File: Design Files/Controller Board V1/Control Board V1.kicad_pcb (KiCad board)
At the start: 4 copper layers, 75 x 125 mm, 72 parts, among them J1 XT30PW-F, J10 SM04B-GHS-TB_LF__SN_-, J11 SM04B-GHS-TB_LF__SN_-, J2 XT30UPB-M, J3 XT30UPB-M, J4 XT30UPB-M, J5 XT30UPB-M, J6 XT30UPB-M, J7 XT30UPB-M, J8 SM04B-GHS-TB_LF__SN_-, J9 SM04B-GHS-TB_LF__SN_-, Q1 LMG5200, U1 LMR51420XDDCR, U2 INA219BIDR, U3 INA219BIDR, U4 INA219BIDR, U5 SC0917

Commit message: small issues fixed
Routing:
- net 5V: track 13.0 -> 16.4 mm, vias 20 -> 22
- net P_GND: track 30.8 -> 33.7 mm

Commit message: some stuff
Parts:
- moved C2 3.30 mm to (121.5, 102.7)
- moved C3 3.30 mm to (121.5, 110.7)
- moved Q1 3.30 mm to (118.7, 106.7)
- moved R13 3.30 mm to (123.7, 105.2)
- moved R14 3.30 mm to (123.7, 108.2)
- moved C4 3.30 mm to (123.1, 73.0)
- moved J1 3.30 mm to (124.6, 65.1)
- moved R2 3.30 mm to (116.8, 77.5)
- moved R3 3.30 mm to (125.8, 79.0)
- moved R4 3.30 mm to (125.8, 77.5)
- moved U2 3.30 mm to (121.6, 77.5)
- moved C1 3.13 mm to (113.5, 79.0)
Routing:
- net 5V: track 16.4 -> 7.37 mm
- net /PWM_bottom: track 26.9 -> 28.4 mm
- net /I2C_current_SDA: track 110.6 -> 109.3 mm
- net /I2C_current_SCL: track 98.1 -> 96.8 mm
- net /PWM_top: track 26.7 -> 27.9 mm
- added copper zone on F.Cu, net Net-(L2-Pad1)

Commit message: finished the stuffs
yippee
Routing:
- net P_GND: track 33.7 -> 30.3 mm, vias 50 -> 51
- net 5V: track 7.37 -> 5.81 mm, vias 22 -> 25
- added copper zone on F.Cu, net /CAP_IN
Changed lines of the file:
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@@
 	(gr_poly
 		(pts
-			(xy 115.260877 75.183181) (xy 118.560877 75.183181) (xy 119.560877 76.183181) (xy 119.760877 76.183181)
-			(xy 119.960877 75.983181) (xy 119.960877 74.183181) (xy 121 69) (xy 121 66.2) (xy 118.2 66.2) (xy 115.260877 73.983181)
+			(xy 115.2 75.183181) (xy 118.560877 75.183181) (xy 119.560877 76.183181) (xy 119.760877 76.183181)
+			(xy 119.960877 75.983181) (xy 119.960877 74) (xy 115.2 74)
 		)
 		(stroke
@@
 		(fill none)
 		(layer "F.Cu")
+	)
+	(gr_poly
+		(pts
+			(xy 121.6 104.9) (xy 121.5 104.8) (xy 121.5 104.4) (xy 121.6 103.6) (xy 121.8 103.2) (xy 121.8 102.3)
+			(xy 122.7 102.3) (xy 122.8 103.3) (xy 122.7 103.5) (xy 122.4 104.6) (xy 122 104.9)
+		)
+		(stroke
+			(width 0.2)
+			(type solid)
+		)
+		(fill solid)
+		(layer "F.Cu")
+		(net 6)
 	)
 	(gr_poly
@@
 	(gr_poly
 		(pts
-			(xy 85.026398 102.139369) (xy 86.597851 100.667569) (xy 88.488581 100.708877) (xy 90.4 102.4) (xy 92.114482 102.455667)
-			(xy 93.473914 102.775615) (xy 93.351264 103.603502) (xy 92.201421 103.603502) (xy 90.706625 102.775616)
-			(xy 88.606244 102.162365) (xy 86.176242 103.250884) (xy 85.23337 103.235553) (xy 85.026398 103.074574)
+			(xy 85.024977 102.135867) (xy 86.59643 100.664067) (xy 88.48716 100.705375) (xy 90.398579 102.396498)
+			(xy 92.113061 102.452165) (xy 93.472493 102.772113) (xy 93.198579 103.496498) (xy 92.2 103.5) (xy 90.705204 102.772114)
+			(xy 88.604823 102.158863) (xy 86.174821 103.247382) (xy 85.231949 103.232051) (xy 85.024977 103.071072)
 		)
 		(stroke
@@
 	(gr_poly
 		(pts
-			(xy 84 104.1) (xy 84.1 106.3) (xy 85.4 106.7) (xy 87.9 106.7) (xy 89.1 105.3) (xy 88.1 102.9) (xy 86.7 103.3)
-			(xy 86.2 103.7) (xy 84.2 103.7)
+			(xy 84.1 106.3) (xy 85.4 106.7) (xy 87.9 106.7) (xy 89.1 105.3) (xy 88.1 102.9) (xy 86.4 103.7) (xy 84.1 103.7)
 		)
 		(stroke
@@
 	)
 	(segment
+		(start 72.045828 115.57)
+		(end 72.045828 116.445828)
+		(width 0.5)
+		(layer "F.Cu")
+		(net 4)
+	)
+	(segment
 		(start 75.36275 77.959613)
 		(end 74.384167 77.959613)
@@
 	)
 	(segment
-		(start 72.045828 115.57)
-		(end 70.194171 115.57)
-		(width 0.5)
-		(layer "F.Cu")
-		(net 4)
-	)
-	(segment
 		(start 85.933334 155.375)
 		(end 85.933334 156.133334)
@@
 	)
 	(segment
+		(start 72.045828 116.445828)
+		(end 72.3 116.7)
+		(width 0.5)
+		(layer "F.Cu")
+		(net 4)
+	)
+	(segment
 		(start 114.070167 156.070167)
 		(end 114.4 156.4)
@@
 	)
 	(segment
-		(start 70.194171 115.57)
-		(end 68.191643 117.572528)
-		(width 0.5)
-		(layer "F.Cu")
-		(net 4)
-	)
-	(segment
 		(start 120.675 104.075)
 		(end 120.75 104.15)
@@
 	)
 	(via blind
+		(at 72.3 116.7)
+		(size 0.6)
+		(drill 0.3)
+		(layers "F.Cu" "In1.Cu")
+		(net 4)
+	)
+	(via blind
 		(at 73.504631 57.396411)
 		(size 0.6)
@@
 		(net 5)
 	)
-	(segment
-		(start 122.225 103.875)
-		(end 121.95 104.15)
-		(width 0.5)
-		(layer "F.Cu")
-		(net 6)
-	)
-	(segment
-		(start 122.225 102.7)
-		(end 122.225 103.875)
-		(width 0.5)
-		(layer "F.Cu")
-		(net 6)
-	)
 	(via blind
 		(at 79 102.9)
@@
 	)
 	(via blind
+		(at 121.9 103.5)
+		(size 0.6)
+		(drill 0.3)
+		(layers "F.Cu" "In2.Cu")
+		(free yes)
+		(net 6)
+	)
+	(via blind
 		(at 125.4 75.7)
 		(size 0.6)
@@
 	)
 	(via blind
+		(at 121.8 104.6)
+		(size 0.6)
+		(drill 0.3)
+		(layers "F.Cu" "In2.Cu")
+		(free yes)
+		(net 6)
+	)
+	(via blind
 		(at 126.1 76.3)
+		(size 0.6)
+		(drill 0.3)
+		(layers "F.Cu" "In2.Cu")
+		(free yes)
+		(net 6)
+	)
+	(via blind
+		(at 122.5 103.3)
 		(size 0.6)
 		(drill 0.3)
@@
 	)
 	(segment
-		(start 88.288929 104.994196)
+		(start 89.379778 104.879778)
+		(end 88.288929 103.788929)
+		(width 0.5)
+		(layer "F.Cu")
+		(net 28)
+	)
+	(segment
+		(start 88.288929 103.788929)
 		(end 88.288929 101.79877)
 		(width 0.5)
@@
 	(segment
 		(start 89.379778 106.085045)
-		(end 88.288929 104.994196)
+		(end 89.379778 104.879778)
 		(width 0.5)
 		(layer "F.Cu")
@@
 			(pts
 				(xy 76.8 108.9) (xy 76.8 113.3) (xy 76.8 122.1) (xy 83.6 122.1) (xy 99.5 122.1) (xy 99.5 120.5)
-				(xy 99.9 119.9) (xy 101 118.8) (xy 119.3 118.8) (xy 119.3 108.6) (xy 91.3 108.6) (xy 87.9 105) (xy 87.9 103.1)
-				(xy 85.1 103.1) (xy 82.7 103.1) (xy 82.6 108.9)
+				(xy 99.9 119.9) (xy 101 118.8) (xy 119.3 118.8) (xy 119.3 108.6) (xy 91.3 108.6) (xy 87.9 105) (xy 87.9 102.8)
+				(xy 82.6 102.8) (xy 82.6 108.9)
 			)
 		)
@@
 	)
 	(zone
+		(net 7)
+		(net_name "/CAP_IN")
+		(layer "F.Cu")
+		(hatch none 0.5)
+		(priority 1)
+		(connect_pads yes
+			(clearance 0)
+		)
+		(min_thickness 0.25)
+		(filled_areas_thickness no)
+		(fill yes
+			(thermal_gap 0.5)
+			(thermal_bridge_width 0.5)
+			(island_removal_mode 1)
+			(island_area_min 10)
+		)
+		(polygon
+			(pts
+				(xy 115.2 75.183181) (xy 119.960877 74) (xy 121.1 69.1) (xy 121.1 66.1) (xy 118.2 66.1) (xy 114.8 67)
+				(xy 113 73.4)
+			)
+		)
+	)
+	(zone
 		(net 4)
 		(net_name "P_GND")
@@
 		(polygon
 			(pts
-				(xy 123 101.5) (xy 123.5 103.2) (xy 122.4 105) (xy 108 105) (xy 108 101.5)
+				(xy 122.8 101.5) (xy 123.5 103.2) (xy 122.8 105) (xy 108 105) (xy 108 101.5)
 			)
 		)
@@
 			"583f4df7-8fac-4cbd-82ce-f205a44a597c" "5d9e4cb1-e675-4766-86f6-c9fbc5cd8f8f"
 			"5e24a0d1-ffb5-4ccc-8d19-4f8c13946d0e" "5e960d50-e155-412f-96fc-e3142376b7e8"
-			"68d7e094-cd08-4d67-b0e3-78303260dc1e" "6cf498db-3432-45d3-8c32-362254403798"
+			"640729bb-d87d-45f8-bb5f-7fb30d67480c" "6cf498db-3432-45d3-8c32-362254403798"
 			"6fcb1b68-7ee1-4a5c-99de-65e6fa297009" "7524d766-485d-4db8-82db-5c5d20982b83"
 			"76bea91c-fd3f-49b3-8351-fa2908513b24" "79fb91fa-d631-46f4-a465-6aafe271f5f5"
-			"8b0a0997-ac0a-4843-9d3c-7aba647cdfc4" "97e8f3d6-9ae4-49f6-9d14-747fa14f0a50"
+			"7f770451-475f-427e-a839-d25e019b1486" "8b0a0997-ac0a-4843-9d3c-7aba647cdfc4"
+			"94de7636-d79e-4243-8107-30afec6cb93c" "97e8f3d6-9ae4-49f6-9d14-747fa14f0a50"
 			"9b16b59e-c7ed-471c-910c-8daa297b2831" "9cac112b-d2e7-4d06-8906-c0670bea4c48"
 			"a3925c4d-db26-45a8-88d8-d9c2b1d4682e" "a7862c28-294d-4fba-864e-b5acfd495a3a"
 			"a9f3f0e8-963c-4c59-be1b-b4fcc45b154f" "abc72818-2439-4c0e-8367-a4768fb89b16"
-			"b2158cf1-eb62-44fc-acc6-f40ad1d21d73" "bded6fd2-167c-4a3c-b67c-34651a94f9e5"
+			"b2158cf1-eb62-44fc-acc6-f40ad1d21d73" "be421fbe-92af-480e-a00a-106512b46463"
 			"c198362b-c47e-4b00-a246-c995cf1e92e2" "c75d7a87-7e86-44d0-86e0-ba194b234927"
 			"cbc1f7fa-b2af-4bee-b431-f5128f3fc790" "ce336664-c232-4bd1-8327-4e3bc8ae5cfa"
@@
 			"330b5346-ee03-4ccb-a2e8-f70af065349e" "362cf553-4c6f-44a3-814f-9aafacb7149e"
 			"3786135e-dc1e-46f8-adb4-22b06da3b455" "37a72350-153e-4021-9f44-709499478770"
-			"37ac942c-c820-4023-ac99-d4c7229de39a" "3943b47c-c5f9-4d98-839c-defade32b3d6"
-			"3a7ffc72-b672-41e5-9450-376bbc01c79b" "46a726ba-56ee-4520-b2d3-d4d7cdf6566b"
-			"526b88f3-1dab-422e-893f-1b2c01fe874f" "546cac1f-572f-49ff-8702-6f9544b5b6f2"
-			"5c8aaf3b-7e70-4f96-a209-0fc7e1262841" "62601344-9b4f-4d08-9275-5624dfc40f33"
-			"62b2ec5d-2978-4c0b-a0d9-f369fb6edd4d" "66176771-d532-460d-93e4-c4fcde17ff9b"
-			"6632844a-c0a0-48b9-bddc-6fd729e13e40" "681d5738-adf9-4486-84c9-fdf01cff44b9"
-			"69719426-1875-4073-a496-a9386f5beb8f" "6d70b5e3-2cca-49e6-a7e6-5546aec6c352"
-			"735188d5-e988-40c1-8d32-c965199fea6d" "74bf968a-2eb9-4f31-815a-4a151dd0e82c"
-			"7740900c-165d-4e62-abd3-4689b696aaf7" "7b525c96-2723-4a41-9cee-f33cf8efd5d7"
+			"3943b47c-c5f9-4d98-839c-defade32b3d6" "3a7ffc72-b672-41e5-9450-376bbc01c79b"
+			"46a726ba-56ee-4520-b2d3-d4d7cdf6566b" "526b88f3-1dab-422e-893f-1b2c01fe874f"
+			"546cac1f-572f-49ff-8702-6f9544b5b6f2" "5c8aaf3b-7e70-4f96-a209-0fc7e1262841"
+			"62601344-9b4f-4d08-9275-5624dfc40f33" "62b2ec5d-2978-4c0b-a0d9-f369fb6edd4d"
+			"66176771-d532-460d-93e4-c4fcde17ff9b" "6632844a-c0a0-48b9-bddc-6fd729e13e40"
+			"681d5738-adf9-4486-84c9-fdf01cff44b9" "69719426-1875-4073-a496-a9386f5beb8f"
+			"6d70b5e3-2cca-49e6-a7e6-5546aec6c352" "735188d5-e988-40c1-8d32-c965199fea6d"
+			"74bf968a-2eb9-4f31-815a-4a151dd0e82c" "7740900c-165d-4e62-abd3-4689b696aaf7"
+			"7b525c96-2723-4a41-9cee-f33cf8efd5d7" "852520d6-c01d-43c5-833f-3cd822acd1ff"
 			"91e29a2a-0354-4217-9fe5-f18d4fc59a33" "929ccb9c-92e4-48f6-b01b-3d6677283a92"
-			"930d19a7-7ff0-43f8-81db-066a22cfd5d8" "9964af3c-70ab-4abc-a192-2d251fe86dcc"
-			"9c4b813d-05e7-4548-99e3-6bd1e0cfc629" "add65acd-046f-4b91-86c8-98b1c4fdc4e6"
-			"b511fa1b-357b-4564-84c1-3b721654b8a4" "bafa75cc-7183-468d-bc32-5838b034c9e0"
-			"bd9d6ae3-a2b4-44e1-8bc5-4617d19f2927" "c0a86e8a-b530-47ee-adc4-3694f0d68c0c"
+			"9964af3c-70ab-4abc-a192-2d251fe86dcc" "9da1f060-4254-4a97-a122-ef85e1ae045d"
+			"add65acd-046f-4b91-86c8-98b1c4fdc4e6" "b511fa1b-357b-4564-84c1-3b721654b8a4"
+			"bafa75cc-7183-468d-bc32-5838b034c9e0" "bd9d6ae3-a2b4-44e1-8bc5-4617d19f2927"
+			"c0a86e8a-b530-47ee-adc4-3694f0d68c0c" "c64881d7-e3d4-458c-9106-d891b6cdeaca"
 			"ca964e1e-3cbf-4d6f-ab18-995f1eb3b613" "cb251945-bc11-4f8c-b3d5-1a0f0acfe6df"
-			"d557426c-c26f-4910-9769-4f95ad23c57a" "d931bb5b-1f4b-4898-9407-32404f2cc3c5"
-			"dd631645-3c7b-411d-a646-2cce025b4d8e" "ea4476a5-22ed-4662-be9f-8f747a3393b9"
-			"fa4dea38-8a01-4e5f-a42f-c25cac921510" "fda227e2-c579-4f73-88de-f4c77bf80f8c"
-			"fec5a4e1-a340-4ce4-a8c0-8198ab5b11f2"
-		)
-	)
+			"d557426c-c26f-4910-9769-4f95ad23c57a" "d7c146f3-868d-4ef2-9568-6037358f73d9"
+			"d931bb5b-1f4b-4898-9407-32404f2cc3c5" "dd631645-3c7b-411d-a646-2cce025b4d8e"
+			"ea4476a5-22ed-4662-be9f-8f747a3393b9" "fa4dea38-8a01-4e5f-a42f-c25cac921510"
+			"fda227e2-c579-4f73-88de-f4c77bf80f8c" "fec5a4e1-a340-4ce4-a8c0-8198ab5b11f2"
+		)
+	)

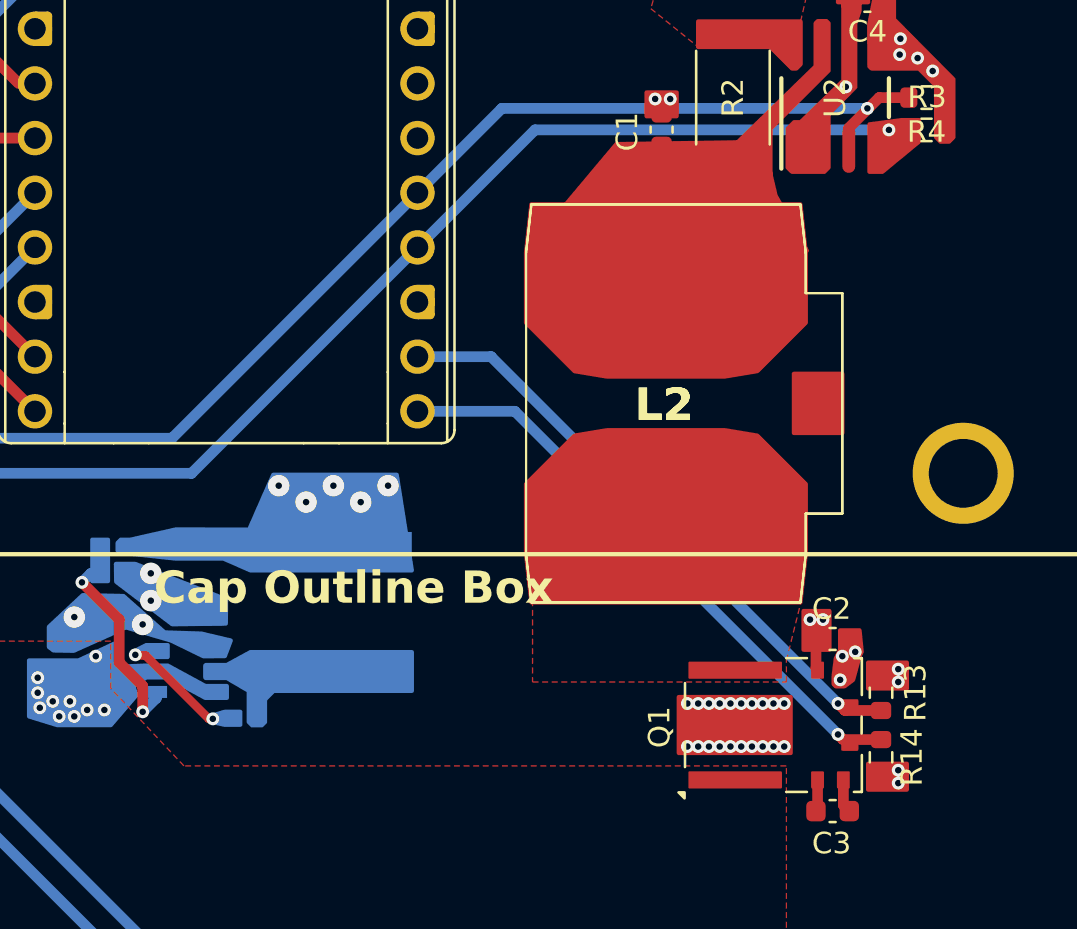
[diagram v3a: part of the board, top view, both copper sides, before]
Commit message: tweaked 5v to q1
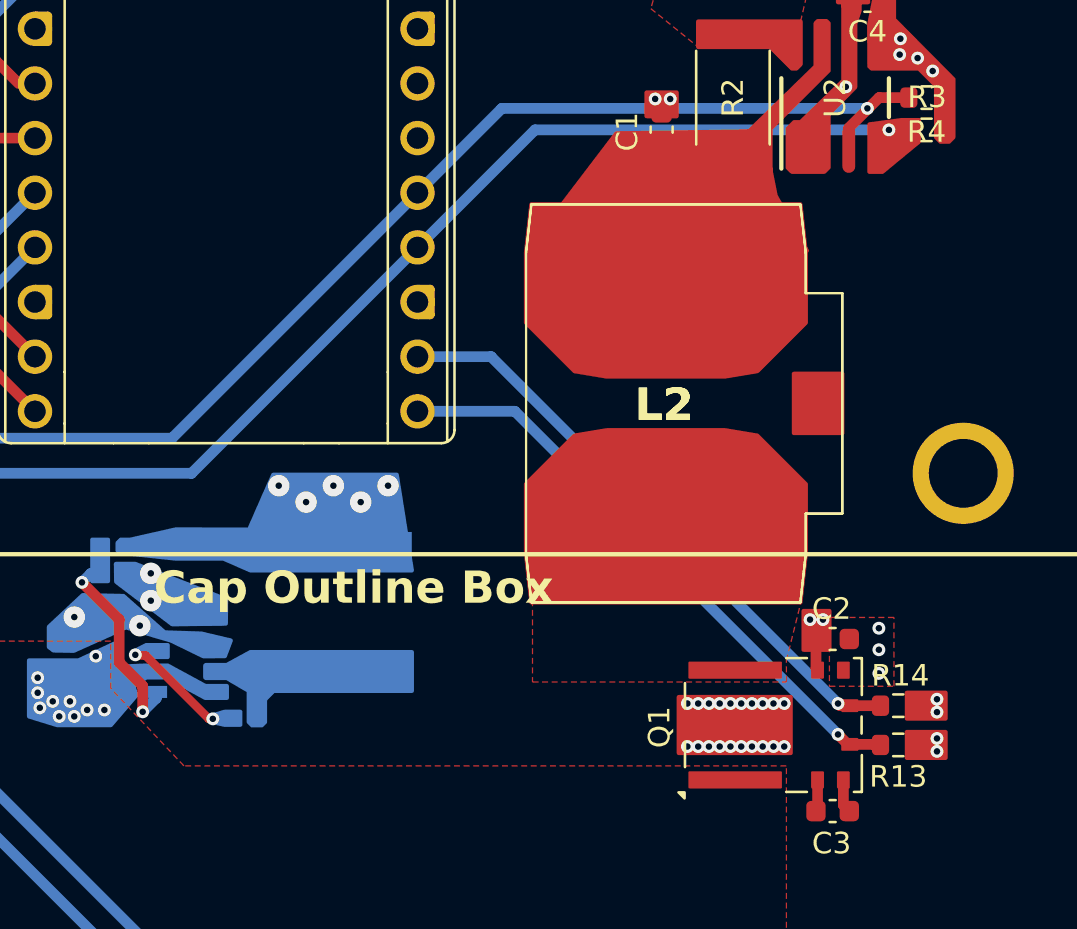
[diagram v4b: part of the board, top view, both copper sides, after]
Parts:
- moved R13 1.00 mm to (124.5, 105.8), turned to 0 degrees
- moved R14 0.99 mm to (124.5, 107.6), turned to 0 degrees
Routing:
- added copper zone on F.Cu, net 5V

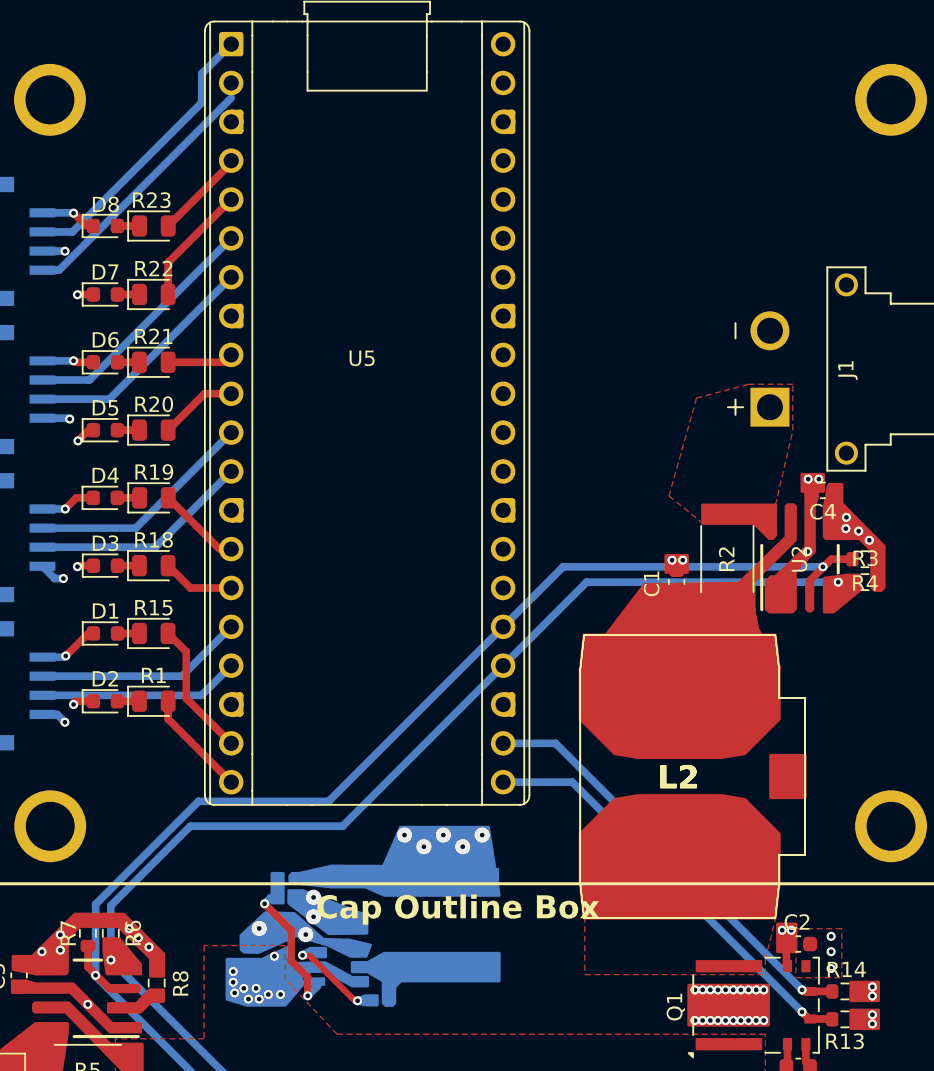
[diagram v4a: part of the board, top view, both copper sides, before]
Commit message: Added i2c level shifter
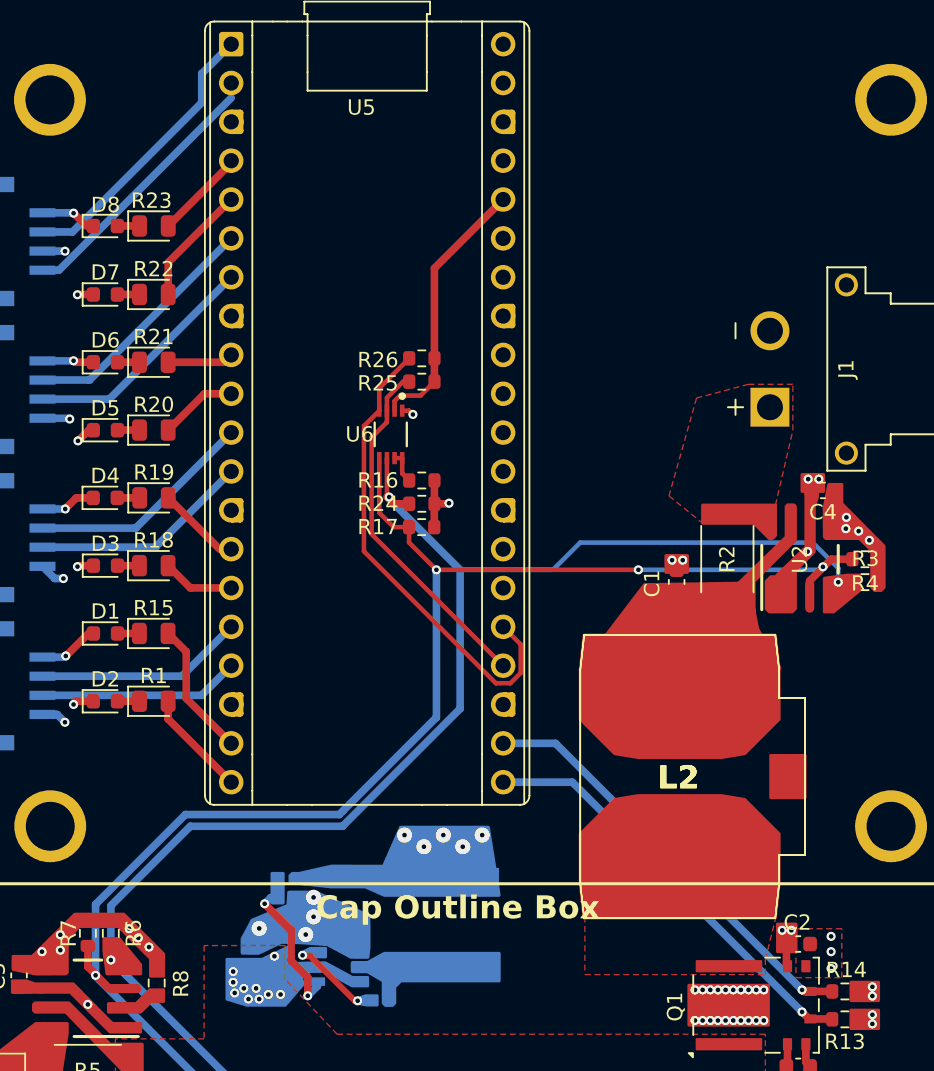
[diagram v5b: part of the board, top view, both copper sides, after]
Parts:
- added R16: 200k, PGA460TW:R_0603_1608Metric, F.Cu at (96.8, 72.4)
- added R17: 10k, PGA460TW:R_0603_1608Metric, F.Cu at (96.8, 75.4)
- added R24: 10k, PGA460TW:R_0603_1608Metric, F.Cu at (96.8, 73.9)
- added R25: 10k, PGA460TW:R_0603_1608Metric, F.Cu at (96.8, 65.9)
- added R26: 10k, PGA460TW:R_0603_1608Metric, F.Cu at (96.8, 64.4)
- added U6: TCA39306DCUR, PGA460TW:DCU0008A-MFG, F.Cu at (94.8, 69.4)
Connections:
- C1 pad 1: P_GND -> A_GND
- C10 pad 1: P_GND -> A_GND
- C11 pad 1: P_GND -> A_GND
- C2 pad 2: P_GND -> A_GND
- C4 pad 2: P_GND -> A_GND
- C7 pad 1: P_GND -> A_GND
- C8 pad 1: P_GND -> A_GND
- C9 pad 1: P_GND -> A_GND
- Cin1 pad 2: P_GND -> A_GND
- Cinx1 pad 2: P_GND -> A_GND
- Cout1 pad 2: D_GND -> A_GND
- D1 pad 1: P_GND -> A_GND
- D2 pad 1: P_GND -> A_GND
- D3 pad 1: P_GND -> A_GND
- D4 pad 1: P_GND -> A_GND
- D5 pad 1: P_GND -> A_GND
- D6 pad 1: P_GND -> A_GND
- D7 pad 1: P_GND -> A_GND
- D8 pad 1: P_GND -> A_GND
- J1 pad N: P_GND -> A_GND
- J10 pad 4: P_GND -> A_GND
- J11 pad 4: P_GND -> A_GND
- J2 pad N: P_GND -> A_GND
- J3 pad N: P_GND -> A_GND
- J4 pad N: P_GND -> A_GND
- J5 pad N: P_GND -> A_GND
- J6 pad N: P_GND -> A_GND
- J7 pad N: P_GND -> A_GND
- J8 pad 2: P_GND -> A_GND
- J8 pad 4: P_GND -> A_GND
- J9 pad 4: P_GND -> A_GND
- Q1 pad 7: P_GND -> A_GND
- Q1 pad 9: P_GND -> A_GND
- R13 pad 2: P_GND -> A_GND
- R14 pad 2: P_GND -> A_GND
- Rfbb1 pad 2: D_GND -> A_GND
- U1 pad 1: P_GND -> A_GND
- U5 pad 13: P_GND -> A_GND
- U5 pad 18: P_GND -> A_GND
- U5 pad 23: P_GND -> A_GND
- U5 pad 24: /I2C_current_SCL -> Net-(U5-GP18)
- U5 pad 25: /I2C_current_SDA -> Net-(U5-GP19)
- U5 pad 28: P_GND -> A_GND
- U5 pad 3: P_GND -> A_GND
- U5 pad 33: P_GND -> A_GND
- U5 pad 38: P_GND -> A_GND
- U5 pad 8: P_GND -> A_GND
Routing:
- net Net-(U5-GP19): track 0.00 -> 31.4 mm
- net A_GND: track 0.00 -> 31.3 mm, vias 0 -> 52
- net P_GND: track 30.3 -> 0.00 mm, vias 51 -> 0
- net Net-(U5-GP18): track 0.00 -> 23.5 mm
- net /I2C_current_SCL: track 96.8 -> 115.8 mm, vias 3 -> 4
- net 3.3V: track 0.00 -> 17.5 mm
- net /I2C_current_SDA: track 109.3 -> 124.4 mm, vias 3 -> 5
- net 5V: track 5.81 -> 9.83 mm, vias 25 -> 26
- net Net-(U6-EN): track 0.00 -> 2.15 mm
- added copper zone on In1.Cu, net A_GND
- removed copper zone on In1.Cu, net P_GND
